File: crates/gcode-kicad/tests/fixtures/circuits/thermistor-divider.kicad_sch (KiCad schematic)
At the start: 2 parts

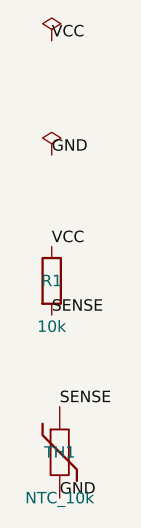
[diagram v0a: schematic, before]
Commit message: KiCad 10: real ERC 10/10 PASS, v10 format tokens, fix symbol-library drift
Environment moved to KiCad 10.0.7, which unblocked tasks 1.1/1.2 and surfaced a
real defect:

- catalog: Device:Q_NMOS_GSD no longer exists in KiCad 10; the replacement
  Device:Q_NMOS uses LETTER pin numbers (D/G/S). The stale entry silently fell
  back to the 2-pin generic stub, and the stub made ERC report PASS - a false
  pass. Fixed, plus two guard tests (every lib_id must resolve; every referenced
  pin must exist on its symbol) and the acceptance harness now refuses to count
  a stub-substituted circuit (exit 4).
- schematic: emit the KiCad 10 format (version 20260306, generator_version 10.0,
  quoted uuids, body_style/exclude_from_sim/in_pos_files, (hide yes) property
  form) so the declared format matches the embedded v10 symbol definitions.
- fixtures regenerated; 89 tests green
- KR1: 10/10 on all four measurable tracks (generate, symbol resolution,
  KiCad netlist exact, ERC PASS) vs target >= 7
- docs: PRD appendix and tasks.md updated; 44/44 tasks complete
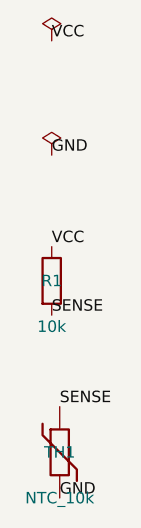
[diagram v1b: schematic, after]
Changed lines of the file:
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@@
 (kicad_sch
-  (version 20230121)
-  (generator gcode)
+  (version 20260306)
+  (generator "gcode")
+  (generator_version "10.0")
   (paper "A4")
   (title_block (title "Gcode generated"))
@@
     (at 77.216 53.34 0)
     (unit 1)
-    (in_bom yes)
-    (on_board yes)
+    (body_style 1)
+    (exclude_from_sim no)
+    (in_bom yes)
+    (on_board yes)
+    (in_pos_files yes)
     (dnp no)
     (property
@@
       "#FLG1"
       (at 77.216 53.34 0)
-      (effects (font (size 1.27 1.27)) hide)
+      (hide yes)
+      (show_name no)
+      (do_not_autoplace no)
+      (effects (font (size 1.27 1.27)))
     )
     (property
@@
       "PWR_FLAG"
       (at 77.216 58.42 0)
-      (effects (font (size 1.27 1.27)) hide)
+      (hide yes)
+      (show_name no)
+      (do_not_autoplace no)
+      (effects (font (size 1.27 1.27)))
     )
     (property
@@
       ""
       (at 77.216 60.96 0)
-      (effects (font (size 1.27 1.27)) hide)
+      (hide yes)
+      (show_name no)
+      (do_not_autoplace no)
+      (effects (font (size 1.27 1.27)))
     )
     (property
@@
       ""
       (at 77.216 63.5 0)
-      (effects (font (size 1.27 1.27)) hide)
+      (hide yes)
+      (show_name no)
+      (do_not_autoplace no)
+      (effects (font (size 1.27 1.27)))
     )
     (pin "1")
@@
     (at 77.216 66.04 0)
     (unit 1)
-    (in_bom yes)
-    (on_board yes)
+    (body_style 1)
+    (exclude_from_sim no)
+    (in_bom yes)
+    (on_board yes)
+    (in_pos_files yes)
     (dnp no)
     (property
@@
       "#FLG2"
       (at 77.216 66.04 0)
-      (effects (font (size 1.27 1.27)) hide)
+      (hide yes)
+      (show_name no)
+      (do_not_autoplace no)
+      (effects (font (size 1.27 1.27)))
     )
     (property
@@
       "PWR_FLAG"
       (at 77.216 71.12 0)
-      (effects (font (size 1.27 1.27)) hide)
+      (hide yes)
+      (show_name no)
+      (do_not_autoplace no)
+      (effects (font (size 1.27 1.27)))
     )
     (property
@@
       ""
       (at 77.216 73.66 0)
-      (effects (font (size 1.27 1.27)) hide)
+      (hide yes)
+      (show_name no)
+      (do_not_autoplace no)
+      (effects (font (size 1.27 1.27)))
     )
     (property
@@
       ""
       (at 77.216 76.2 0)
-      (effects (font (size 1.27 1.27)) hide)
+      (hide yes)
+      (show_name no)
+      (do_not_autoplace no)
+      (effects (font (size 1.27 1.27)))
     )
     (pin "1")
@@
     (at 77.216 80.01 0)
     (unit 1)
-    (in_bom yes)
-    (on_board yes)
+    (body_style 1)
+    (exclude_from_sim no)
+    (in_bom yes)
+    (on_board yes)
+    (in_pos_files yes)
     (dnp no)
     (property
@@
       "R1"
       (at 77.216 80.01 0)
+      (show_name no)
+      (do_not_autoplace no)
       (effects (font (size 1.27 1.27)))
     )
@@
       "10k"
       (at 77.216 85.09 0)
+      (show_name no)
+      (do_not_autoplace no)
       (effects (font (size 1.27 1.27)))
     )
@@
       ""
       (at 77.216 87.63 0)
-      (effects (font (size 1.27 1.27)) hide)
+      (hide yes)
+      (show_name no)
+      (do_not_autoplace no)
+      (effects (font (size 1.27 1.27)))
     )
     (property
@@
       ""
       (at 77.216 90.17 0)
-      (effects (font (size 1.27 1.27)) hide)
+      (hide yes)
+      (show_name no)
+      (do_not_autoplace no)
+      (effects (font (size 1.27 1.27)))
     )
     (pin "1")
@@
     (at 78.105 99.06 0)
     (unit 1)
-    (in_bom yes)
-    (on_board yes)
+    (body_style 1)
+    (exclude_from_sim no)
+    (in_bom yes)
+    (on_board yes)
+    (in_pos_files yes)
     (dnp no)
     (property
@@
       "TH1"
       (at 78.105 99.06 0)
+      (show_name no)
+      (do_not_autoplace no)
       (effects (font (size 1.27 1.27)))
     )
@@
       "NTC_10k"
       (at 78.105 104.14 0)
+      (show_name no)
+      (do_not_autoplace no)
       (effects (font (size 1.27 1.27)))
     )
@@
       ""
       (at 78.105 106.68 0)
-      (effects (font (size 1.27 1.27)) hide)
+      (hide yes)
+      (show_name no)
+      (do_not_autoplace no)
+      (effects (font (size 1.27 1.27)))
     )
     (property
@@
       ""
       (at 78.105 109.22 0)
-      (effects (font (size 1.27 1.27)) hide)
-    )
-    (pin "1")
+      (hide yes)
+      (show_name no)
+      (do_not_autoplace no)
+      (effects (font (size 1.27 1.27)))
+    )
+    (pin "1")

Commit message: R1: gcode-sim crate — SPICE netlist generation, ngspice driver, metric analysis
New crate crates/gcode-sim:
- models: lib_id -> SPICE card + behavioural macromodels (LM321 single-pole
  opamp, Q_NMOS level-1, LED, L7805, thermistor); unknown devices are rejected
- netlist: deterministic deck from NetlistIr; GND -> node 0, sanitised node names
  with collision detection, stimuli from the analysis config, wrdata control block
- runner: ngspice probe/version gate, batch execution, waveform retrieval parsed
  BY COLUMN NAME (which is what makes .op's placeholder scale column harmless)
- analysis: pure metric extraction (dc, gain, shape-aware -3dB, rise time,
  ripple, min/max) plus expectation checking with Chinese explanations
- artifacts: deterministic CSV and dependency-free SVG (Bode + time domain)
- recipes: 11 recipes over all 10 catalog circuits with analytically derived
  expectations and documented tolerances

Real findings from actually simulating (all fixed):
- non-inverting-amp was wired for gain 1.11, not 10.1 (feedback resistors swapped)
- MOSFETs need the M card, not Q (Q is a BJT); bulk ties to source
- ngspice level-1 MOS rejects Cgs/Cgd (wants CGSO/CGDO)
- ngspice vp() returns radians, not degrees
- with the switch off, the drain is a floating node; measure the supply side
- Sallen-Key Q was 0.34 (overdamped) -> values swapped for Q~0.74
- thermistor value must be numeric to be simulatable

Acceptance: 11/11 recipes, 12/12 metrics PASS against ngspice-42; R0 still
10/10 KR1 and 146 workspace tests green.
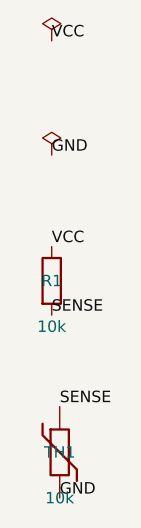
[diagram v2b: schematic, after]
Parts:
- TH1: value NTC_10k -> 10k
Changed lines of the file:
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@@
     (instances (project
   "gcode"
-  (path "/4e748cc1-c6a3-5ca7-bb6e-af8026ef96bb" (reference "#FLG1") (unit 1))
+  (path "/9e83a926-3be2-5c98-80cd-ffae68907a90" (reference "#FLG1") (unit 1))
 ))
   )
@@
     (instances (project
   "gcode"
-  (path "/4e748cc1-c6a3-5ca7-bb6e-af8026ef96bb" (reference "#FLG2") (unit 1))
+  (path "/9e83a926-3be2-5c98-80cd-ffae68907a90" (reference "#FLG2") (unit 1))
 ))
   )
@@
     (instances (project
   "gcode"
-  (path "/4e748cc1-c6a3-5ca7-bb6e-af8026ef96bb" (reference "R1") (unit 1))
+  (path "/9e83a926-3be2-5c98-80cd-ffae68907a90" (reference "R1") (unit 1))
 ))
   )
@@
     (property
       "Value"
-      "NTC_10k"
+      "10k"
       (at 78.105 104.14 0)
       (show_name no)
@@
     (instances (project
   "gcode"
-  (path "/4e748cc1-c6a3-5ca7-bb6e-af8026ef96bb" (reference "TH1") (unit 1))
+  (path "/9e83a926-3be2-5c98-80cd-ffae68907a90" (reference "TH1") (unit 1))
 ))
   )
